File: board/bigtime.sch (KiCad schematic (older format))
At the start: 10 parts, among them IC1 NPIC6C596A, IC2 TPS62152, P1 CONN_IN, P2 CONN_OUT, U1 SA40-19

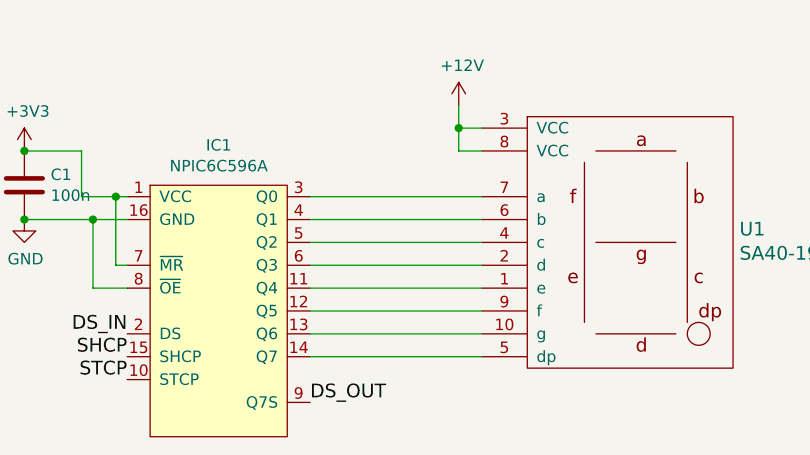
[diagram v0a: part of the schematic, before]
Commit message: Added limit resistors
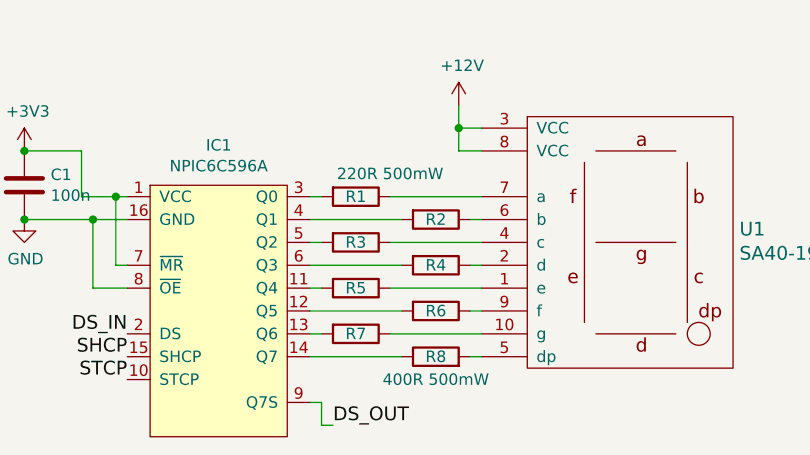
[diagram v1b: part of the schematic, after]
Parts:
- added R1, R2, R3, R4, R5, R6, R7: 220R 500mW, agg:1206, symbol R
- added R8: 400R 500mW, agg:1206, symbol R
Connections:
- net at IC1.11 (Q4): now also R5.2; no longer U1.1 (e)
- net at IC1.12 (Q5): now also R6.2; no longer U1.9 (f)
- net at IC1.13 (Q6): now also R7.2; no longer U1.10 (g)
- net at IC1.14 (Q7): now also R8.1; no longer U1.5 (dp)
- net at IC1.3 (Q0): now also R1.2; no longer U1.7 (a)
- net at IC1.4 (Q1): now also R2.2; no longer U1.6 (b)
- net at IC1.5 (Q2): now also R3.2; no longer U1.4 (c)
- net at IC1.6 (Q3): now also R4.2; no longer U1.2 (d)
- new net: R5.1, U1.1 (e)
- new net: R7.1, U1.10 (g)
- new net: R4.1, U1.2 (d)
- new net: R3.1, U1.4 (c)
- new net: R8.2, U1.5 (dp)
- new net: R2.1, U1.6 (b)
- new net: R1.1, U1.7 (a)
- new net: R6.1, U1.9 (f)
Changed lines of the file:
@@
 LIBS:contrib
 LIBS:valves
-LIBS:npic6c596a
-LIBS:tps62152
 LIBS:sa40-19
 LIBS:bigtime-cache
@@
 $EndComp
 $Comp
-L GND #PWR1
+L GND #PWR6
 U 1 1 58AB653E
 P 3000 1550
-F 0 "#PWR1" H -200 100 50  0001 C CNN
+F 0 "#PWR6" H -200 100 50  0001 C CNN
 F 1 "GND" H 3005 1377 50  0000 C CNN
 F 2 "" H -200 350 50  0000 C CNN
@@
 $EndComp
 $Comp
-L GND #PWR4
+L GND #PWR7
 U 1 1 58AB65DB
 P 3900 1550
-F 0 "#PWR4" H -50 -350 50  0001 C CNN
+F 0 "#PWR7" H -50 -350 50  0001 C CNN
 F 1 "GND" H 3905 1377 50  0000 C CNN
 F 2 "" H -50 -100 50  0000 C CNN
@@
 $EndComp
 $Comp
-L +12V #PWR2
+L +12V #PWR1
 U 1 1 58AB65F8
 P 3250 950
-F 0 "#PWR2" H -250 -400 50  0001 C CNN
+F 0 "#PWR1" H -250 -400 50  0001 C CNN
 F 1 "+12V" H 3265 1123 50  0000 C CNN
 F 2 "" H -250 -250 50  0000 C CNN
@@
 Text Label 5100 4850 2    60   ~ 0
 DS_IN
-Text Label 5900 5150 0    60   ~ 0
+Text Label 6000 5250 0    60   ~ 0
 DS_OUT
 Text Label 3300 1350 0    60   ~ 0
@@
 STCP
 $Comp
-L +3V3 #PWR3
+L +3V3 #PWR2
 U 1 1 58AB6B00
 P 3550 950
-F 0 "#PWR3" H -100 -200 50  0001 C CNN
+F 0 "#PWR2" H -100 -200 50  0001 C CNN
 F 1 "+3V3" H 3565 1123 50  0000 C CNN
 F 2 "" H -100 -50 50  0000 C CNN
@@
 $EndComp
 $Comp
-L +12V #PWR7
+L +12V #PWR3
 U 1 1 58AB6FA8
 P 6000 950
-F 0 "#PWR7" H -600 -450 50  0001 C CNN
+F 0 "#PWR3" H -600 -450 50  0001 C CNN
 F 1 "+12V" H 6015 1123 50  0000 C CNN
 F 2 "" H -600 -300 50  0000 C CNN
@@
 Connection ~ 6500 1250
 $Comp
-L GND #PWR9
+L GND #PWR10
 U 1 1 58AB711C
 P 6500 2350
-F 0 "#PWR9" H 150 -300 50  0001 C CNN
+F 0 "#PWR10" H 150 -300 50  0001 C CNN
 F 1 "GND" H 6505 2177 50  0000 C CNN
 F 2 "" H 150 -50 50  0000 C CNN
@@
 	7500 1450 7500 1850
 $Comp
-L GND #PWR11
+L GND #PWR9
 U 1 1 58AB72DE
 P 7500 1850
-F 0 "#PWR11" H 0   -150 50  0001 C CNN
+F 0 "#PWR9" H 0   -150 50  0001 C CNN
 F 1 "GND" H 7505 1677 50  0000 C CNN
 F 2 "" H 0   100 50  0000 C CNN
@@
 Connection ~ 8350 1050
 $Comp
-L +3V3 #PWR13
+L +3V3 #PWR4
 U 1 1 58AB765A
 P 8700 1000
-F 0 "#PWR13" H 8750 1050 50  0001 C CNN
+F 0 "#PWR4" H 8750 1050 50  0001 C CNN
 F 1 "+3V3" H 8715 1173 50  0000 C CNN
 F 2 "" H -100 -100 50  0000 C CNN
@@
 $EndComp
 $Comp
-L GND #PWR12
+L GND #PWR5
 U 1 1 58AB76DE
 P 8350 1350
-F 0 "#PWR12" H 250 -450 50  0001 C CNN
+F 0 "#PWR5" H 250 -450 50  0001 C CNN
 F 1 "GND" H 8355 1177 50  0000 C CNN
 F 2 "" H 250 -200 50  0000 C CNN
@@
 	4650 4350 5100 4350
 $Comp
-L GND #PWR6
+L GND #PWR13
 U 1 1 58AB81EC
 P 4650 4350
-F 0 "#PWR6" H 250 -950 50  0001 C CNN
+F 0 "#PWR13" H 250 -950 50  0001 C CNN
 F 1 "GND" H 4655 4177 50  0000 C CNN
 F 2 "" H 250 -700 50  0000 C CNN
@@
 	4900 4250 5100 4250
 $Comp
-L +3V3 #PWR5
+L +3V3 #PWR12
 U 1 1 58AB83D7
 P 4650 4050
-F 0 "#PWR5" H 200 -750 50  0001 C CNN
+F 0 "#PWR12" H 200 -750 50  0001 C CNN
 F 1 "+3V3" H 4665 4223 50  0000 C CNN
 F 2 "" H 200 -600 50  0000 C CNN
@@
 $EndComp
 $Comp
-L +12V #PWR10
+L +12V #PWR11
 U 1 1 58AB91CE
 P 6550 3850
-F 0 "#PWR10" H 150 250 50  0001 C CNN
+F 0 "#PWR11" H 150 250 50  0001 C CNN
 F 1 "+12V" H 6565 4023 50  0000 C CNN
 F 2 "" H 150 400 50  0000 C CNN
@@
 	6550 4050 6650 4050
 Connection ~ 6550 3950
-Wire Wire Line
-	5900 4250 6650 4250
-Wire Wire Line
-	6650 4350 5900 4350
-Wire Wire Line
-	5900 4450 6650 4450
-Wire Wire Line
-	6650 4550 5900 4550
-Wire Wire Line
-	5900 4650 6650 4650
-Wire Wire Line
-	6650 4750 5900 4750
-Wire Wire Line
-	5900 4850 6650 4850
-Wire Wire Line
-	6650 4950 5900 4950
+$Comp
+L R R1
+U 1 1 58AC6016
+P 6100 4250
+F 0 "R1" V 6100 4250 50  0000 C CNN
+F 1 "220R 500mW" V 6000 4400 50  0000 C CNN
+F 2 "agg:1206" V 130 450 50  0001 C CNN
+F 3 "" H 200 450 50  0001 C CNN
+	1    6100 4250
+	0    1    1    0
+$EndComp
+$Comp
+L R R8
+U 1 1 58AC6381
+P 6450 4950
+F 0 "R8" V 6450 4950 50  0000 C CNN
+F 1 "400R 500mW" V 6350 4950 50  0000 C CNN
+F 2 "agg:1206" V 480 1150 50  0001 C CNN
+F 3 "" H 550 1150 50  0001 C CNN
+	1    6450 4950
+	0    -1   -1   0
+$EndComp
+Wire Wire Line
+	5900 5150 5950 5150
+Wire Wire Line
+	5950 5150 5950 5250
+Wire Wire Line
+	5950 5250 6000 5250
+Wire Wire Line
+	5900 4250 5950 4250
+Wire Wire Line
+	6250 4250 6650 4250
+Wire Wire Line
+	5900 4350 6300 4350
+Wire Wire Line
+	6600 4350 6650 4350
+Wire Wire Line
+	5900 4450 5950 4450
+Wire Wire Line
+	6250 4450 6650 4450
+Wire Wire Line
+	5900 4550 6300 4550
+Wire Wire Line
+	6600 4550 6650 4550
+Wire Wire Line
+	5900 4650 5950 4650
+Wire Wire Line
+	6250 4650 6650 4650
+Wire Wire Line
+	5900 4750 6300 4750
+Wire Wire Line
+	6600 4750 6650 4750
+Wire Wire Line
+	5900 4850 5950 4850
+Wire Wire Line
+	6250 4850 6650 4850
+Wire Wire Line
+	5900 4950 6300 4950
+Wire Wire Line
+	6600 4950 6650 4950
+$Comp
+L R R2
+U 1 1 58AC75A0
+P 6450 4350
+F 0 "R2" V 6450 4350 50  0000 C CNN
+F 1 "220R 500mW" V 6350 4500 50  0001 C CNN
+F 2 "agg:1206" V 480 550 50  0001 C CNN
+F 3 "" H 550 550 50  0001 C CNN
+	1    6450 4350
+	0    1    1    0
+$EndComp
+$Comp
+L R R3
+U 1 1 58AC76CC
+P 6100 4450
+F 0 "R3" V 6100 4450 50  0000 C CNN
+F 1 "220R 500mW" V 6000 4600 50  0001 C CNN
+F 2 "agg:1206" V 130 650 50  0001 C CNN
+F 3 "" H 200 650 50  0001 C CNN
+	1    6100 4450
+	0    1    1    0
+$EndComp
+$Comp
+L R R4
+U 1 1 58AC7704
+P 6450 4550
+F 0 "R4" V 6450 4550 50  0000 C CNN
+F 1 "220R 500mW" V 6350 4700 50  0001 C CNN
+F 2 "agg:1206" V 480 750 50  0001 C CNN
+F 3 "" H 550 750 50  0001 C CNN
+	1    6450 4550
+	0    1    1    0
+$EndComp
+$Comp
+L R R5
+U 1 1 58AC773E
+P 6100 4650
+F 0 "R5" V 6100 4650 50  0000 C CNN
+F 1 "220R 500mW" V 6000 4800 50  0001 C CNN
+F 2 "agg:1206" V 130 850 50  0001 C CNN
+F 3 "" H 200 850 50  0001 C CNN
+	1    6100 4650
+	0    1    1    0
+$EndComp
+$Comp
+L R R6
+U 1 1 58AC777C
+P 6450 4750
+F 0 "R6" V 6450 4750 50  0000 C CNN
+F 1 "220R 500mW" V 6350 4900 50  0001 C CNN
+F 2 "agg:1206" V 480 950 50  0001 C CNN
+F 3 "" H 550 950 50  0001 C CNN
+	1    6450 4750
+	0    1    1    0
+$EndComp
+$Comp
+L R R7
+U 1 1 58AC77BA
+P 6100 4850
+F 0 "R7" V 6100 4850 50  0000 C CNN
+F 1 "220R 500mW" V 6000 5000 50  0001 C CNN
+F 2 "agg:1206" V 130 1050 50  0001 C CNN
+F 3 "" H 200 1050 50  0001 C CNN
+	1    6100 4850
+	0    1    1    0
+$EndComp
 $EndSCHEMATC

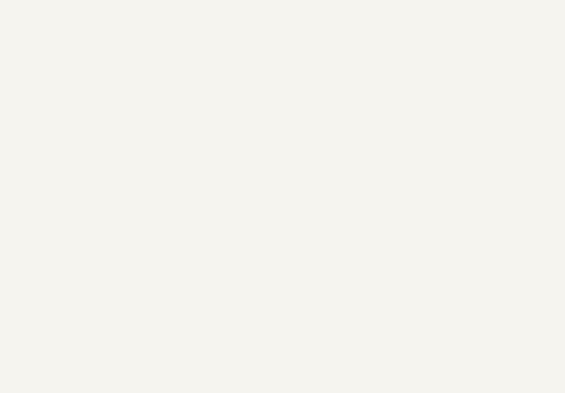
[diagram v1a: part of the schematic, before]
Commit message: Don't forget the mounting holes!
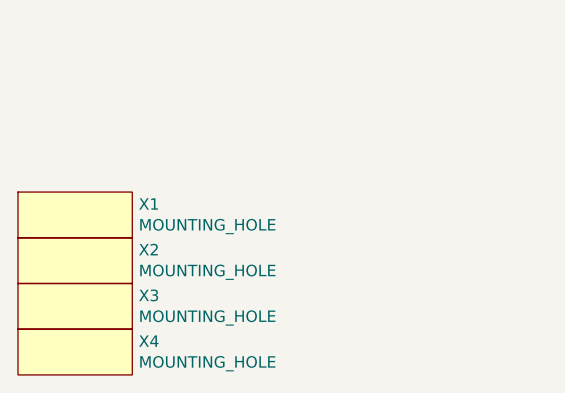
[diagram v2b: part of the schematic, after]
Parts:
- added X1, X2, X3, X4: MOUNTING_HOLE, agg:M3_MOUNT, symbol PART
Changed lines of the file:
@@
 LIBS:valves
 LIBS:sa40-19
+LIBS:part
 LIBS:bigtime-cache
 EELAYER 26 0
@@
 	0    1    1    0
 $EndComp
+$Comp
+L PART X1
+U 1 1 58AC7EDC
+P 1050 6700
+F 0 "X1" H 1578 6796 50  0000 L CNN
+F 1 "MOUNTING_HOLE" H 1578 6705 50  0000 L CNN
+F 2 "agg:M3_MOUNT" H -1950 -550 50  0001 C CNN
+F 3 "" H -1950 -550 50  0001 C CNN
+	1    1050 6700
+	1    0    0    -1
+$EndComp
+$Comp
+L PART X2
+U 1 1 58AC8280
+P 1050 6900
+F 0 "X2" H 1578 6996 50  0000 L CNN
+F 1 "MOUNTING_HOLE" H 1578 6905 50  0000 L CNN
+F 2 "agg:M3_MOUNT" H -1950 -350 50  0001 C CNN
+F 3 "" H -1950 -350 50  0001 C CNN
+	1    1050 6900
+	1    0    0    -1
+$EndComp
+$Comp
+L PART X3
+U 1 1 58AC82C0
+P 1050 7100
+F 0 "X3" H 1578 7196 50  0000 L CNN
+F 1 "MOUNTING_HOLE" H 1578 7105 50  0000 L CNN
+F 2 "agg:M3_MOUNT" H -1950 -150 50  0001 C CNN
+F 3 "" H -1950 -150 50  0001 C CNN
+	1    1050 7100
+	1    0    0    -1
+$EndComp
+$Comp
+L PART X4
+U 1 1 58AC82FE
+P 1050 7300
+F 0 "X4" H 1578 7396 50  0000 L CNN
+F 1 "MOUNTING_HOLE" H 1578 7305 50  0000 L CNN
+F 2 "agg:M3_MOUNT" H -1950 50  50  0001 C CNN
+F 3 "" H -1950 50  50  0001 C CNN
+	1    1050 7300
+	1    0    0    -1
+$EndComp
 $EndSCHEMATC

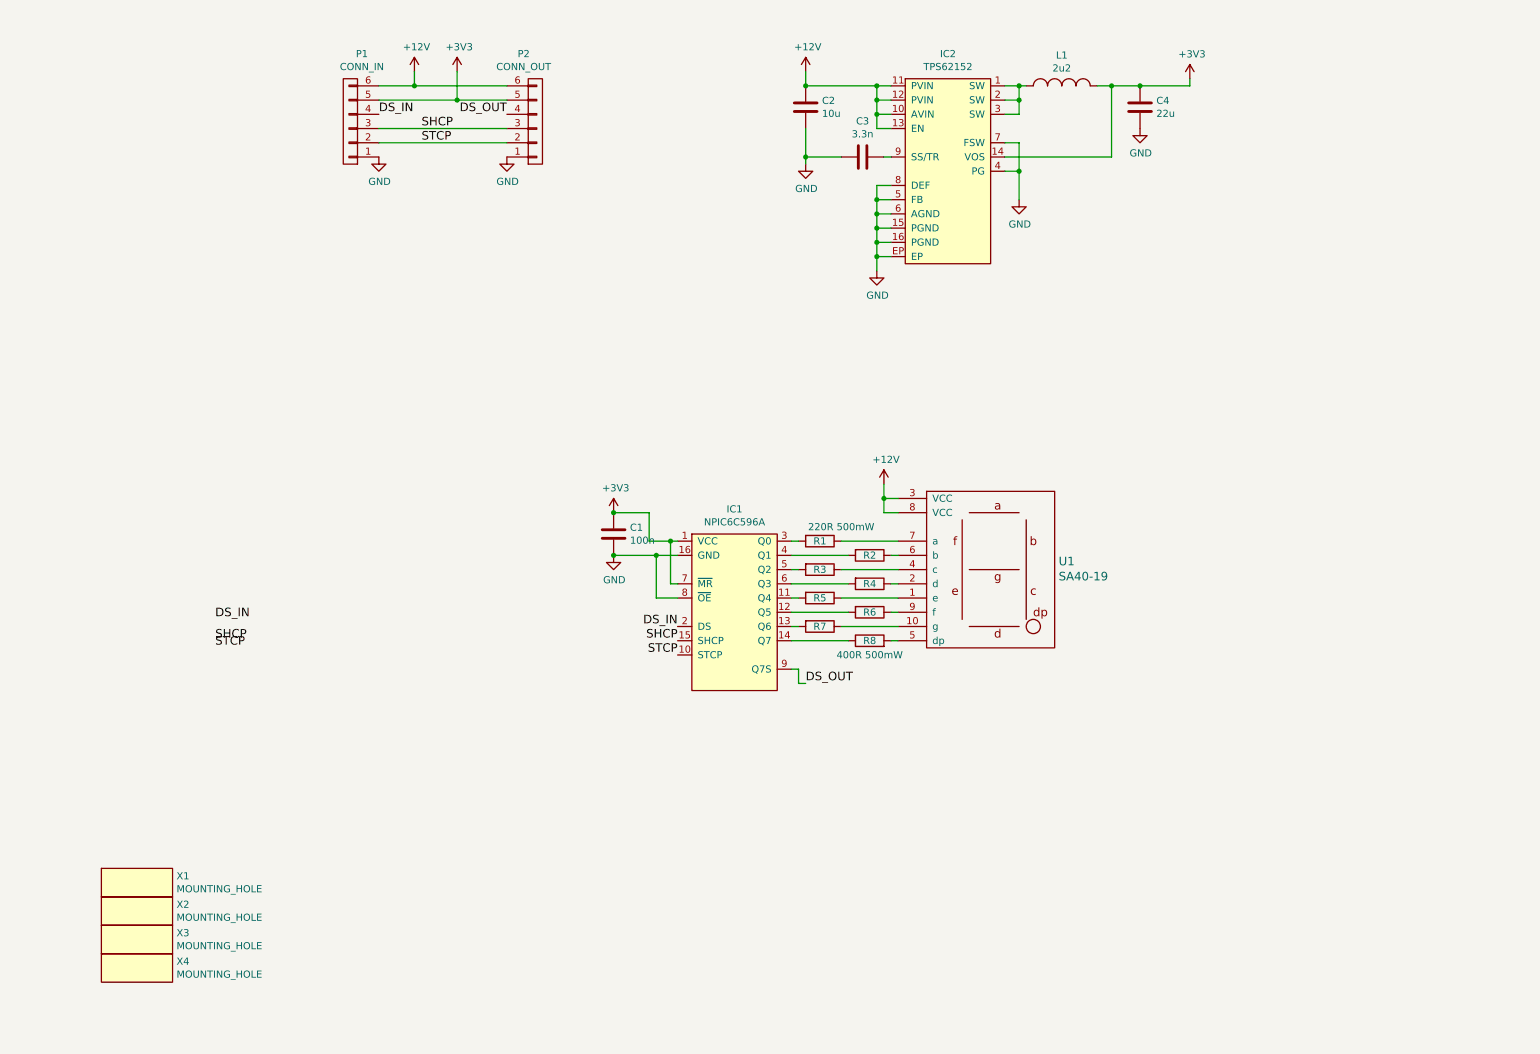
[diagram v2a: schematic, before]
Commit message: added some ethernet bits
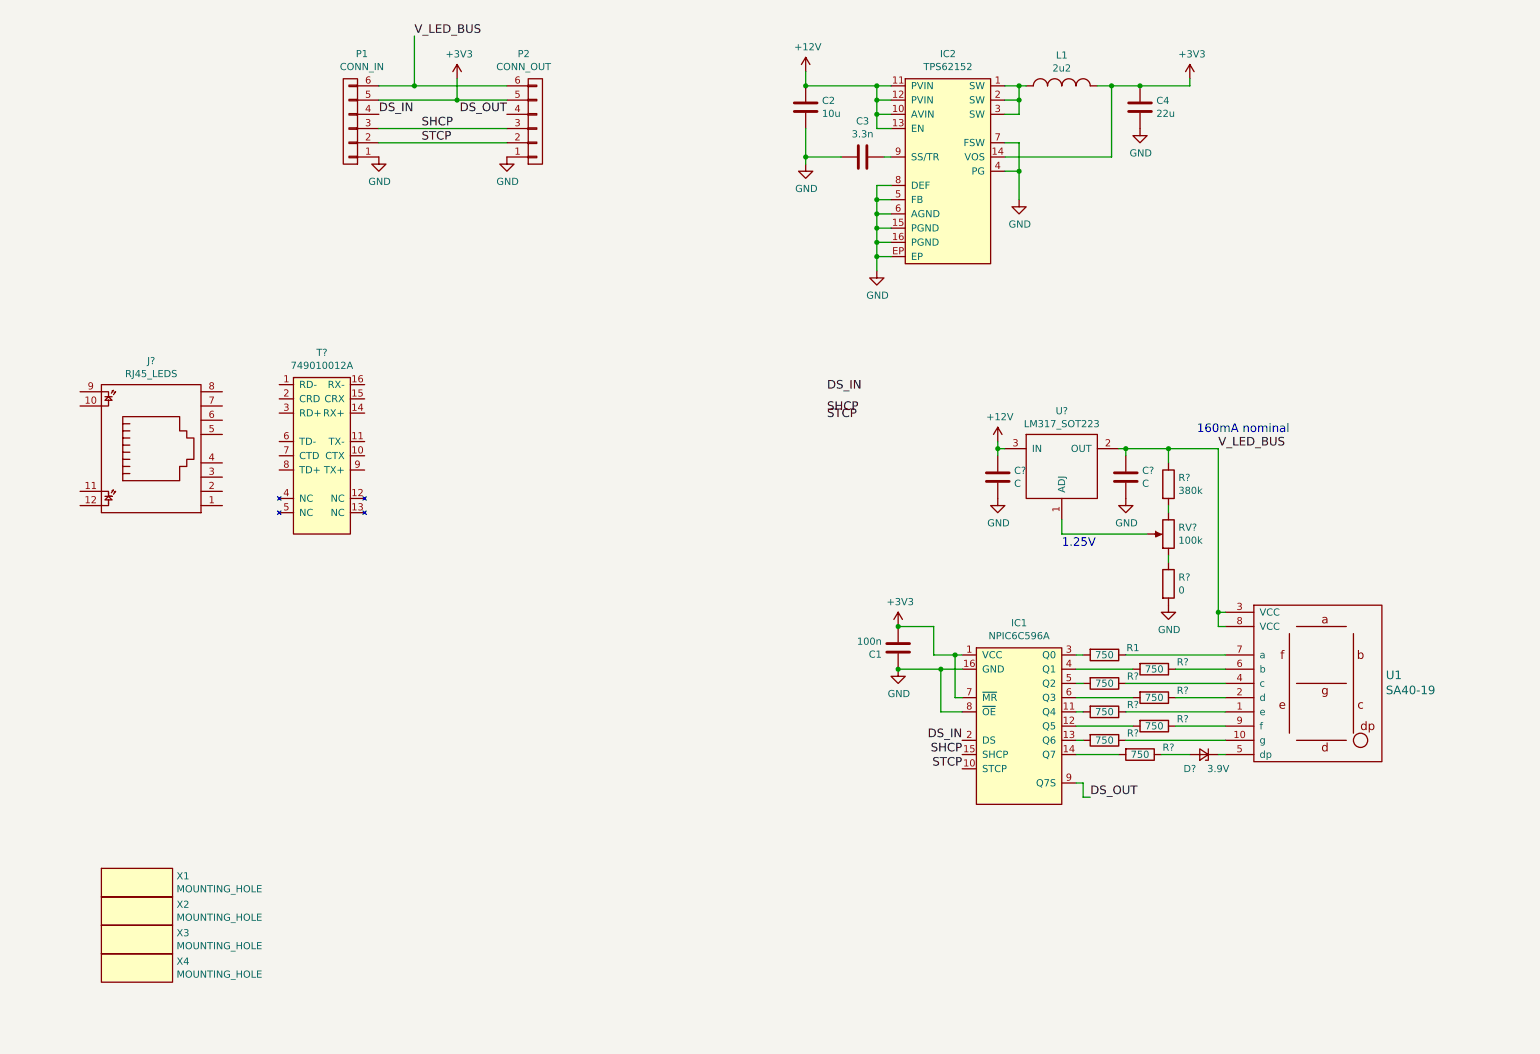
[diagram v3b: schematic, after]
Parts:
- removed R2, R3, R4, R5, R6, R7: 220R 500mW, agg:1206, symbol R
- removed R8: 400R 500mW, agg:1206, symbol R
- added C? (x2): C, symbol C
- added D?: 3.9V, symbol D_Zener_Small
- added J?: RJ45_LEDS, symbol RJ45_LEDS
- added R? (x7): 750, agg:0603, symbol R
- added R?: 380k, symbol R
- added R?: 0, symbol R
- added RV?: 100k, symbol POT
- added T?: 749010012A, agg:749010012A, symbol 749010012A
- added U?: LM317_SOT223, symbol LM317_SOT223
- R1: value 220R 500mW -> 750; footprint agg:1206 -> agg:0603
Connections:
- net +12V: now also C?.2, U?.3 (IN); no longer P1.6 (P6), P2.6 (P6), U1.3 (VCC), U1.8 (VCC)
- net +3V3: now also C1.2; no longer C1.1
- net GND: now also C1.1, C?.1, C?.2, R?.2; no longer C1.2
- net at IC1.11 (Q4): now also R?.2
- net at IC1.12 (Q5): now also R?.2
- net at IC1.13 (Q6): now also R?.2
- net at IC1.14 (Q7): now also R?.2
- net at IC1.4 (Q1): now also R?.2
- net at IC1.5 (Q2): now also R?.2
- net at IC1.6 (Q3): now also R?.2
- net at U1.1 (e): now also R?.1
- net at U1.10 (g): now also R?.1
- net at U1.2 (d): now also R?.1
- net at U1.4 (c): now also R?.1
- net at U1.5 (dp): now also D?.1 (K)
- net at U1.6 (b): now also R?.1
- net at U1.9 (f): now also R?.1
- new net: D?.2 (A), R?.1
- new net: RV?.2, U?.1 (ADJ)
- new net: R?.2, RV?.3
- new net: R?.1, RV?.1
- new net V_LED_BUS: C?.1, P1.6 (P6), P2.6 (P6), R?.1, U1.3 (VCC), U1.8 (VCC), U?.2 (OUT)
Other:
- note added: "1.25V"
- note added: "160mA nominal"
- moved on the sheet: C1, IC1, R1, U1

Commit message: Rescued and fixed library paths
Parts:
- IC2: symbol TPS62152 -> TPS62152-RESCUE-bigtime
- RV?: symbol POT -> POT-RESCUE-bigtime
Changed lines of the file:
@@
 EESchema Schematic File Version 2
+LIBS:bigtime-rescue
 LIBS:power
 LIBS:device
@@
 LIBS:contrib
 LIBS:valves
+LIBS:npic6c596a
+LIBS:tps62152
 LIBS:sa40-19
 LIBS:part
 LIBS:749010012a
+LIBS:ksz8081rnx
 LIBS:bigtime-cache
 EELAYER 26 0
@@
 	3550 1000 3550 1150
 Wire Wire Line
-	3000 1150 3550 1150
-Wire Wire Line
-	3550 1150 3900 1150
+	3000 1150 3900 1150
 Connection ~ 3550 1150
 Wire Wire Line
 	3250 700  3250 1050
 Wire Wire Line
-	3000 1050 3250 1050
-Wire Wire Line
-	3250 1050 3900 1050
+	3000 1050 3900 1050
 Connection ~ 3250 1050
 $Comp
@@
 $EndComp
 $Comp
-L TPS62152 IC2
+L TPS62152-RESCUE-bigtime IC2
 U 1 1 58AB6DDC
 P 7000 1650
@@
 	6000 950  6000 1050
 Wire Wire Line
-	6000 1050 6500 1050
-Wire Wire Line
-	6500 1050 6600 1050
-Wire Wire Line
-	6500 1050 6500 1150
-Wire Wire Line
-	6500 1150 6500 1250
-Wire Wire Line
-	6500 1250 6500 1350
+	6000 1050 6600 1050
+Wire Wire Line
+	6500 1050 6500 1350
 Wire Wire Line
 	6500 1150 6600 1150
@@
 	6500 2250 6600 2250
 Wire Wire Line
-	6500 1750 6500 1850
-Wire Wire Line
-	6500 1850 6500 1950
-Wire Wire Line
-	6500 1950 6500 2050
-Wire Wire Line
-	6500 2050 6500 2150
-Wire Wire Line
-	6500 2150 6500 2250
-Wire Wire Line
-	6500 2250 6500 2350
+	6500 1750 6500 2350
 Wire Wire Line
 	6600 2150 6500 2150
@@
 	7400 1450 7500 1450
 Wire Wire Line
-	7500 1450 7500 1650
-Wire Wire Line
-	7500 1650 7500 1850
+	7500 1450 7500 1850
 $Comp
 L GND #PWR9
@@
 	7500 1250 7400 1250
 Wire Wire Line
-	7500 1050 7500 1150
-Wire Wire Line
-	7500 1150 7500 1250
-Wire Wire Line
-	7400 1050 7500 1050
-Wire Wire Line
-	7500 1050 7550 1050
+	7500 1050 7500 1250
+Wire Wire Line
+	7400 1050 7550 1050
 Connection ~ 7500 1050
 Wire Wire Line
@@
 Connection ~ 7500 1150
 Wire Wire Line
-	8050 1050 8150 1050
-Wire Wire Line
-	8150 1050 8350 1050
-Wire Wire Line
-	8350 1050 8700 1050
+	8050 1050 8700 1050
 Wire Wire Line
 	8150 1050 8150 1550
@@
 $EndComp
 Wire Wire Line
-	6000 1350 6000 1550
-Wire Wire Line
-	6000 1550 6000 1600
+	6000 1350 6000 1600
 Wire Wire Line
 	6250 1550 6000 1550
@@
 $EndComp
 Wire Wire Line
-	6650 5150 6950 5150
-Wire Wire Line
-	6950 5150 7100 5150
+	6650 5150 7100 5150
 $Comp
 L GND #PWR13
@@
 	6900 4850 6900 5050
 Wire Wire Line
-	6900 5050 7050 5050
-Wire Wire Line
-	7050 5050 7100 5050
+	6900 5050 7100 5050
 $Comp
 L +3V3 #PWR12
@@
 $EndComp
 Wire Wire Line
-	7350 3550 7350 3600
-Wire Wire Line
-	7350 3600 7350 3650
+	7350 3550 7350 3650
 Wire Wire Line
 	7350 3600 7400 3600
 Wire Wire Line
-	8200 3600 8250 3600
-Wire Wire Line
-	8250 3600 8550 3600
-Wire Wire Line
-	8550 3600 8900 3600
+	8200 3600 8900 3600
 Wire Wire Line
 	8900 4750 8950 4750
@@
 Connection ~ 8550 3600
 $Comp
-L POT RV?
+L POT-RESCUE-bigtime RV?
 U 1 1 58B7266E
 P 8550 4200
@@
 	7800 4200 7800 4100
 Wire Wire Line
-	8900 3600 8900 4750
-Wire Wire Line
-	8900 4750 8900 4850
+	8900 3600 8900 4850
 Text Label 8900 3600 0    60   ~ 0
 V_LED_BUS
